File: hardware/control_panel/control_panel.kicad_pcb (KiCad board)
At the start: 2 copper layers, 13.5 x 21.5 mm, 2 parts, among them SW1 RotaryEncoder_Switch_MP

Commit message: KiCad updates and EC11 to TWT
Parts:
- removed SW1: RotaryEncoder_Switch_MP, Rotary_Encoder:RotaryEncoder_Alps_EC11E-Switch_Vertical_H20mm
- added 5VGND1: Conn_01x02_Pin, Connector_JST:JST_XH_B2B-XH-A_1x02_P2.50mm_Vertical, F.Cu at (53.3, 53.0)
- added R1: 10k, Resistor_THT:R_Axial_DIN0204_L3.6mm_D1.6mm_P5.08mm_Horizontal, F.Cu at (123.1, 36.5)
- added R2: 10k, Resistor_THT:R_Axial_DIN0204_L3.6mm_D1.6mm_P5.08mm_Horizontal, F.Cu at (123.1, 39.7)
- added R3: 10k, Resistor_THT:R_Axial_DIN0204_L3.6mm_D1.6mm_P5.08mm_Horizontal, F.Cu at (123.1, 42.9)
- added RELAY_2CH_1: Conn_01x04_Pin, Connector_PinHeader_2.54mm:PinHeader_1x04_P2.54mm_Vertical, F.Cu at (54.5, 80.9)
- added ST7789_Socket1: Conn_01x08_Socket, Connector_PinSocket_2.54mm:PinSocket_1x08_P2.54mm_Horizontal, F.Cu at (116.0, 77.4)
- added SW_Cancel_Reset1: SW_Push, Button_Switch_THT:SW_PUSH_6mm_H8.5mm, F.Cu at (100.5, 55.3)
- added SW_Start_Stop_Adjust1: RotaryEncoder_Switch_MP, Rotary_Encoder:RotaryEncoder_Alps_EC11E-Switch_Vertical_H20mm, F.Cu at (92.6, 72.4)
- moved ESPMC1 12.6 mm to (64.5, 68.5), turned to 90 degrees
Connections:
- ESPMC1 pad 1: unconnected-(ESPMC1-GP1-Pad1) -> /IN1_FAN
- ESPMC1 pad 10: unconnected-(ESPMC1-GP10-Pad10) -> /LCD_RST
- ESPMC1 pad 11: unconnected-(ESPMC1-GP11-Pad11) -> /LCD_SDA
- ESPMC1 pad 12: unconnected-(ESPMC1-GP12-Pad12) -> /LCD_SCL
- ESPMC1 pad 2: unconnected-(ESPMC1-GP2-Pad2) -> /IN2_LEDS
- ESPMC1 pad 3V3: unconnected-(ESPMC1-3V3(OUT)-Pad3V3) -> /3V3+
- ESPMC1 pad 4: unconnected-(ESPMC1-GP4-Pad4) -> Net-(ESPMC1-GP4)
- ESPMC1 pad 5: unconnected-(ESPMC1-GP5-Pad5) -> Net-(ESPMC1-GP5)
- ESPMC1 pad 5V: unconnected-(ESPMC1-Pad5V) -> Net-(5VGND1-Pin_1)
- ESPMC1 pad 6: unconnected-(ESPMC1-GP6-Pad6) -> Net-(ESPMC1-GP6)
- ESPMC1 pad 7: unconnected-(ESPMC1-GP7-Pad7) -> Net-(ESPMC1-GP7)
- ESPMC1 pad 8: unconnected-(ESPMC1-GP8-Pad8) -> /LCD_BL
- ESPMC1 pad 9: unconnected-(ESPMC1-GP9-Pad9) -> /LCD_DC
- ESPMC1 pad GND: unconnected-(ESPMC1-PadGND) -> GND
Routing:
- net /3V3+: track 0.00 -> 55.9 mm, vias 0 -> 1
- net Net-(5VGND1-Pin_1): track 0.00 -> 8.31 mm, vias 0 -> 1
- net GND: track 0.00 -> 8.29 mm, vias 0 -> 1
- net /IN2_LEDS: track 0.00 -> 4.81 mm, vias 0 -> 1
- net /IN1_FAN: track 0.00 -> 4.76 mm, vias 0 -> 1
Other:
- board size 13.5 x 21.5 mm -> 70 x 37 mm

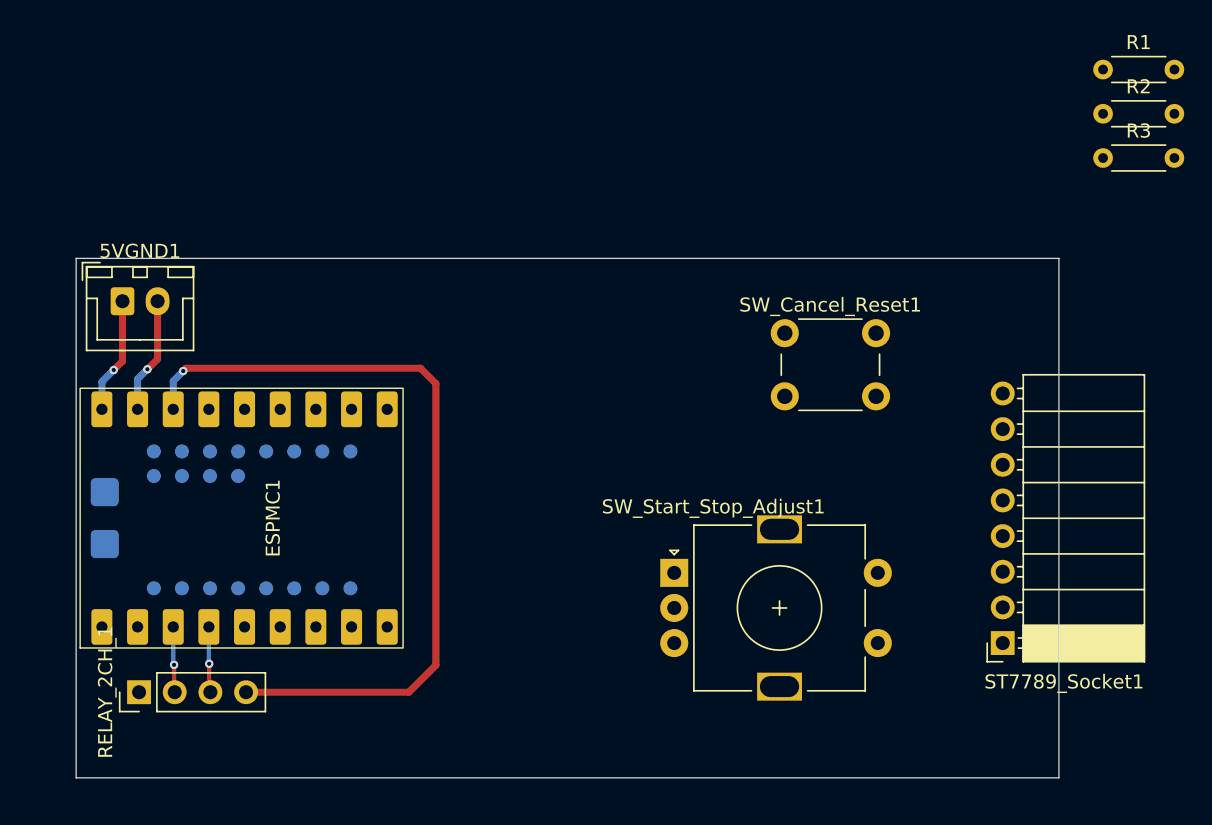
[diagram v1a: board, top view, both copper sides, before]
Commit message: KiCad and python script for stitching PCB layers into one SVG for printing
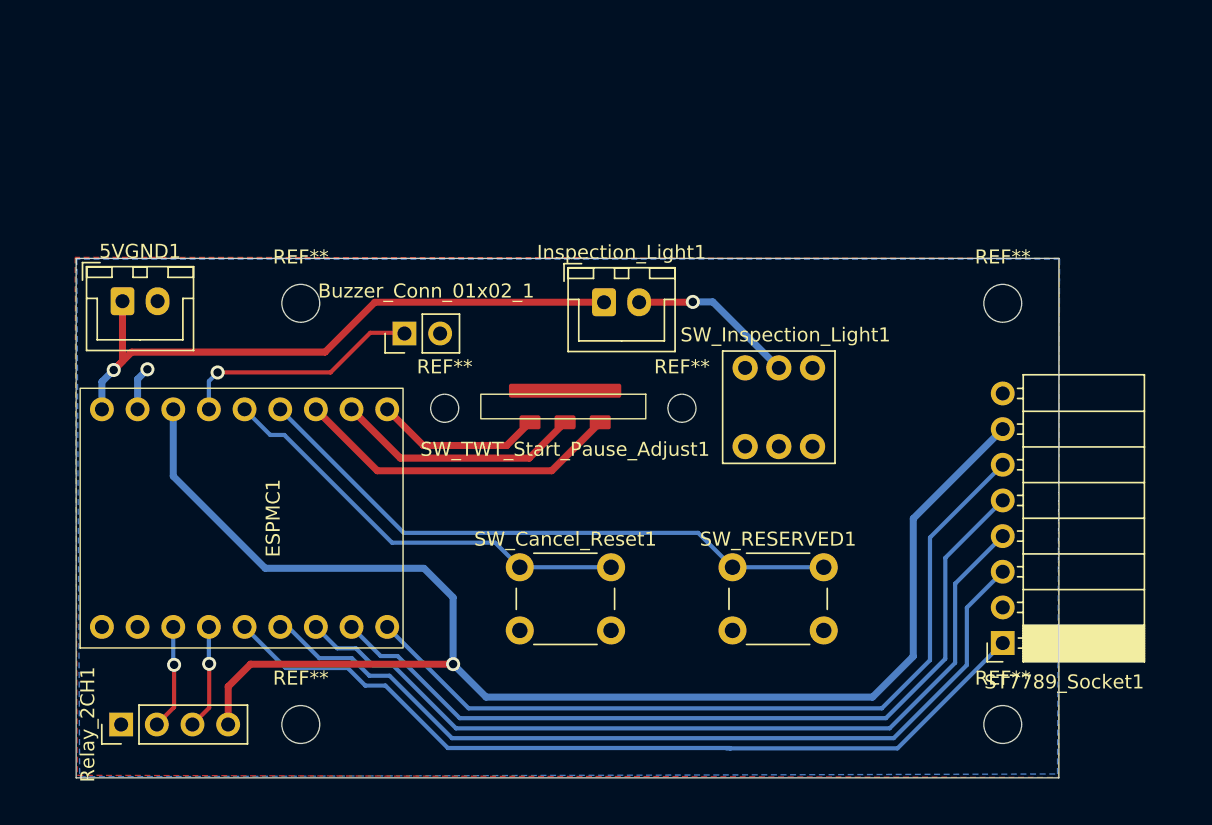
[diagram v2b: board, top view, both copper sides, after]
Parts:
- removed R1, R2, R3: 10k, Resistor_THT:R_Axial_DIN0204_L3.6mm_D1.6mm_P5.08mm_Horizontal
- removed SW_Start_Stop_Adjust1: RotaryEncoder_Switch_MP, Rotary_Encoder:RotaryEncoder_Alps_EC11E-Switch_Vertical_H20mm
- added Buzzer_Conn_01x02_1: Buzzer, Connector_PinHeader_2.54mm:PinHeader_1x02_P2.54mm_Vertical, F.Cu at (73.4, 55.4)
- added Inspection_Light1: Conn_01x02_Socket, Connector_JST:JST_XH_B2B-XH-A_1x02_P2.50mm_Vertical, F.Cu at (87.6, 53.1)
- added REF**: MountingHole_2mm, MountingHole:MountingHole_2mm, F.Cu at (76.2, 60.7)
- added REF**: MountingHole_2.7mm_M2.5_DIN965, MountingHole:MountingHole_2.7mm_M2.5_DIN965, F.Cu at (116.0, 83.2)
- added REF**: MountingHole_2.7mm_M2.5_DIN965, MountingHole:MountingHole_2.7mm_M2.5_DIN965, F.Cu at (66.0, 53.2)
- added REF**: MountingHole_2.7mm_M2.5_DIN965, MountingHole:MountingHole_2.7mm_M2.5_DIN965, F.Cu at (116.0, 53.2)
- added REF**: MountingHole_2.7mm_M2.5_DIN965, MountingHole:MountingHole_2.7mm_M2.5_DIN965, F.Cu at (66.0, 83.2)
- added REF**: MountingHole_2mm, MountingHole:MountingHole_2mm, F.Cu at (93.2, 60.7)
- added SW_Inspection_Light1: SW_Push_DPDT, TMB_Library:SW_Push_DPDT_8x8mm, F.Cu at (100.0, 60.6)
- added SW_RESERVED1: SW_Push, Button_Switch_THT:SW_PUSH_6mm_H8.5mm, F.Cu at (96.8, 72.0)
- added SW_TWT_Start_Pause_Adjust1: ~, TMB_Library:SW_ThumbWheelToggle, F.Cu at (84.8, 60.7)
- ESPMC1: footprint TMB_Library:ESP32-S3_Super_Mini -> TMB_Library:ESP32-S3_Super_Mini_THTONLY
- moved SW_Cancel_Reset1 25.2 mm to (81.6, 72.0)
- moved Relay_2CH1 2.63 mm to (53.2, 83.2)
- renumbered RELAY_2CH_1 to Relay_2CH1
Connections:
- net Net-(5VGND1-Pin_1) renamed /+5V
- ESPMC1 pad 10: /LCD_RST -> /WH_DIR2
- ESPMC1 pad 11: /LCD_SDA -> /RESERVED
- ESPMC1 pad 12: /LCD_SCL -> /CNCL_RSET
- ESPMC1 pad 13: unconnected-(ESPMC1-GP13-Pad13) -> /BUZZER
- ESPMC1 pad 3: unconnected-(ESPMC1-GP3-Pad3) -> /LCD_BL
- ESPMC1 pad 4: Net-(ESPMC1-GP4) -> /LCD_DC
- ESPMC1 pad 5: Net-(ESPMC1-GP5) -> /LCD_RST
- ESPMC1 pad 6: Net-(ESPMC1-GP6) -> /LCD_SDA
- ESPMC1 pad 7: Net-(ESPMC1-GP7) -> /LCD_SCL
- ESPMC1 pad 8: /LCD_BL -> /WH_DIR1
- ESPMC1 pad 9: /LCD_DC -> /WH_SW
- SW_Cancel_Reset1 pad 1: GND -> /CNCL_RSET
- SW_Cancel_Reset1 pad 2: Net-(ESPMC1-GP4) -> GND
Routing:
- net /LCD_DC: track 0.00 -> 62.1 mm
- net /LCD_BL: track 0.00 -> 61.0 mm
- net /LCD_RST: track 0.00 -> 60.9 mm
- net /LCD_SDA: track 0.00 -> 59.7 mm
- net /LCD_SCL: track 0.00 -> 58.5 mm
- net /3V3+: track 55.9 -> 106.2 mm
- net /RESERVED: track 0.00 -> 43.5 mm
- net /+5V: track 8.31 -> 45.2 mm
- net /CNCL_RSET: track 0.00 -> 30.8 mm
- net /WH_DIR2: track 0.00 -> 23.5 mm
- net /WH_SW: track 0.00 -> 17.7 mm
- net /BUZZER: track 0.00 -> 17.4 mm, vias 0 -> 1
- net /WH_DIR1: track 0.00 -> 11.9 mm
- net /INSP_LIGHT_GND: track 0.00 -> 11.9 mm, vias 0 -> 1
- net GND: track 8.29 -> 3.14 mm
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- added copper zone on B.Cu, net GND
- added copper zone on F.Cu, net GND

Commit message: KiCad design fixes and Kicad pcb export fixes
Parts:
- Inspection_Light1: footprint Connector_JST:JST_XH_B2B-XH-A_1x02_P2.50mm_Vertical -> Connector_PinHeader_2.54mm:PinHeader_1x02_P2.54mm_Vertical
- moved Relay_2CH1 58.4 mm to (108.6, 64.6), turned to 0 degrees
- moved Inspection_Light1 21.0 mm to (108.6, 54.2)
- moved REF** 3.00 mm to (63.0, 53.2)
- moved REF** 3.00 mm to (63.0, 83.2)
- moved SW_Cancel_Reset1 2.01 mm to (81.2, 74.0)
- moved SW_RESERVED1 2.00 mm to (96.8, 74.0)
- renumbered ESPMC1 to ESP32-S3SM1
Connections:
- ESP32-S3SM1 pad 1: /IN1_FAN -> /RESERVED
- ESP32-S3SM1 pad 10: /WH_DIR2 -> /WH_DIR1
- ESP32-S3SM1 pad 11: /RESERVED -> /IN1_FAN
- ESP32-S3SM1 pad 12: /CNCL_RSET -> /IN2_LEDS
- ESP32-S3SM1 pad 2: /IN2_LEDS -> /CNCL_RSET
- ESP32-S3SM1 pad 3: /LCD_BL -> /LCD_SCL
- ESP32-S3SM1 pad 4: /LCD_DC -> /LCD_SDA
- ESP32-S3SM1 pad 6: /LCD_SDA -> /LCD_DC
- ESP32-S3SM1 pad 7: /LCD_SCL -> /LCD_BL
- ESP32-S3SM1 pad 8: /WH_DIR1 -> /WH_DIR2
- Inspection_Light1 pad 1: /+5V -> /INSP_LITE_5+
- Inspection_Light1 pad 2: /INSP_LIGHT_GND -> GND
- ST7789_Socket1 pad 1: /LCD_BL -> GND
- ST7789_Socket1 pad 2: GND -> /3V3+
- ST7789_Socket1 pad 3: /LCD_DC -> /LCD_SCL
- ST7789_Socket1 pad 4: /LCD_RST -> /LCD_SDA
- ST7789_Socket1 pad 5: /LCD_SDA -> /LCD_RST
- ST7789_Socket1 pad 6: /LCD_SCL -> /LCD_DC
- ST7789_Socket1 pad 7: /3V3+ -> GND
- ST7789_Socket1 pad 8: GND -> /LCD_BL
- SW_Cancel_Reset1 pad 1: /CNCL_RSET -> GND
- SW_Cancel_Reset1 pad 2: GND -> /CNCL_RSET
- SW_Inspection_Light1 pad 4: GND -> /INSP_LITE_5+
- SW_Inspection_Light1 pad 5: /INSP_LIGHT_GND -> /+5V
- SW_RESERVED1 pad 1: /RESERVED -> GND
- SW_RESERVED1 pad 2: GND -> /RESERVED
- SW_TWT_Start_Pause_Adjust1 pad 1: /WH_DIR2 -> /WH_DIR1
- SW_TWT_Start_Pause_Adjust1 pad 3: /WH_DIR1 -> /WH_DIR2
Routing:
- net /IN2_LEDS: track 7.57 -> 50.3 mm, vias 1 -> 0
- net /3V3+: track 106.2 -> 66.3 mm
- net /IN1_FAN: track 7.55 -> 46.8 mm, vias 1 -> 0
- net /+5V: track 45.2 -> 59.6 mm
- net /INSP_LIGHT_GND: track 11.9 -> 0.00 mm, vias 1 -> 0
- net /WH_DIR2: track 23.5 -> 11.9 mm
- net /WH_DIR1: track 11.9 -> 23.5 mm
- net /INSP_LITE_5+: track 0.00 -> 8.66 mm, vias 0 -> 1
- net /LCD_SCL: track 58.5 -> 65.8 mm, vias 0 -> 1
- net /RESERVED: track 43.5 -> 49.0 mm, vias 0 -> 1
- net /LCD_SDA: track 59.7 -> 65.2 mm, vias 0 -> 1
- net GND: track 3.14 -> 8.29 mm
- net /LCD_BL: track 61.0 -> 63.6 mm, vias 0 -> 1
- net /LCD_RST: track 60.9 -> 63.4 mm, vias 0 -> 1
- net /BUZZER: track 17.4 -> 16.2 mm, vias 1 -> 0
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
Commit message: Minimum vias - 0.3mm tracks
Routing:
- net /RESERVED: track 49.0 -> 50.1 mm, vias 1 -> 0
- net /CNCL_RSET: track 30.4 -> 31.2 mm, vias 1 -> 0
- net /+5V: track 59.6 -> 60.4 mm, vias 1 -> 0
- net /3V3+: track 66.3 -> 65.6 mm, vias 1 -> 0
- net /INSP_LITE_5+: track 8.66 -> 8.94 mm, vias 1 -> 0
- net /LCD_SDA: vias 1 -> 0
- net /LCD_SCL: vias 1 -> 0
- net GND: vias 1 -> 0
- net /LCD_RST: vias 1 -> 0
- net /LCD_DC: vias 1 -> 0
- net /LCD_BL: vias 1 -> 0

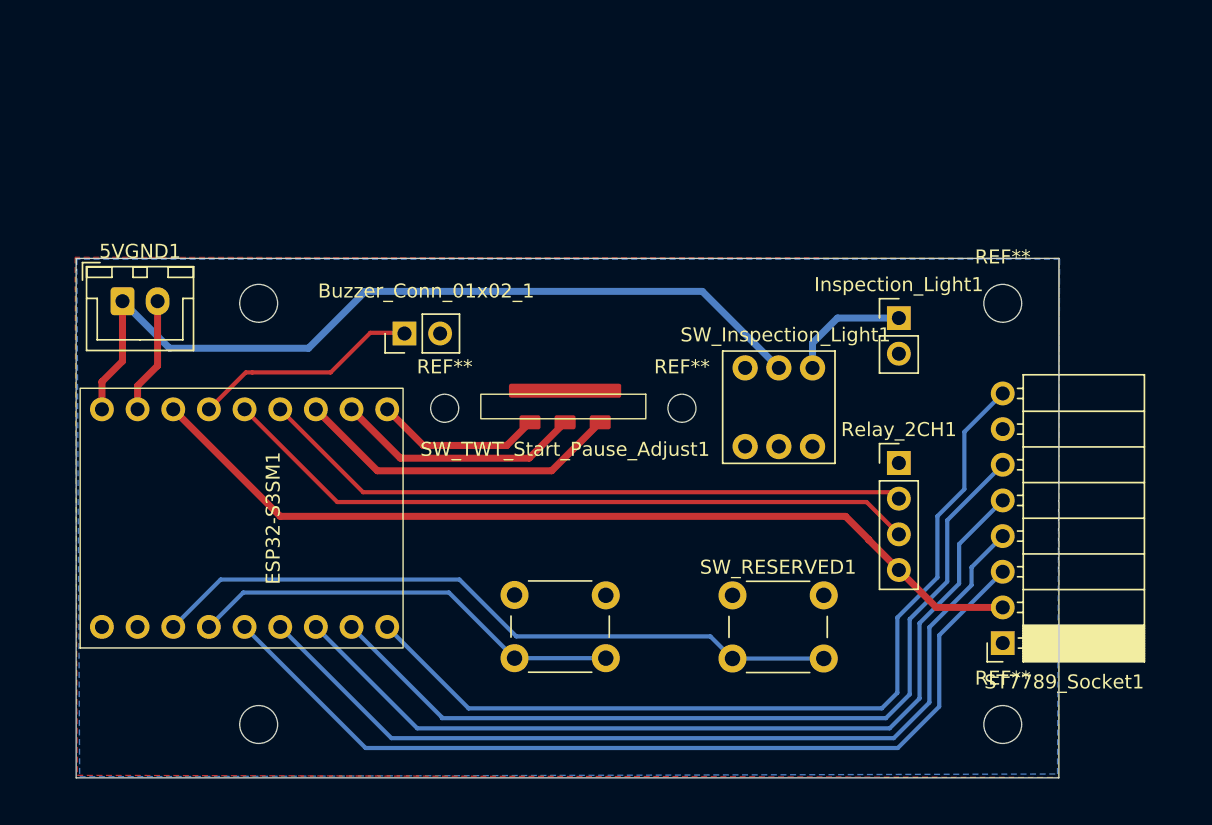
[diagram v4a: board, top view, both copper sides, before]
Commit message: Kicad - Mimimum Vias + 0.5mm min track width + script changes
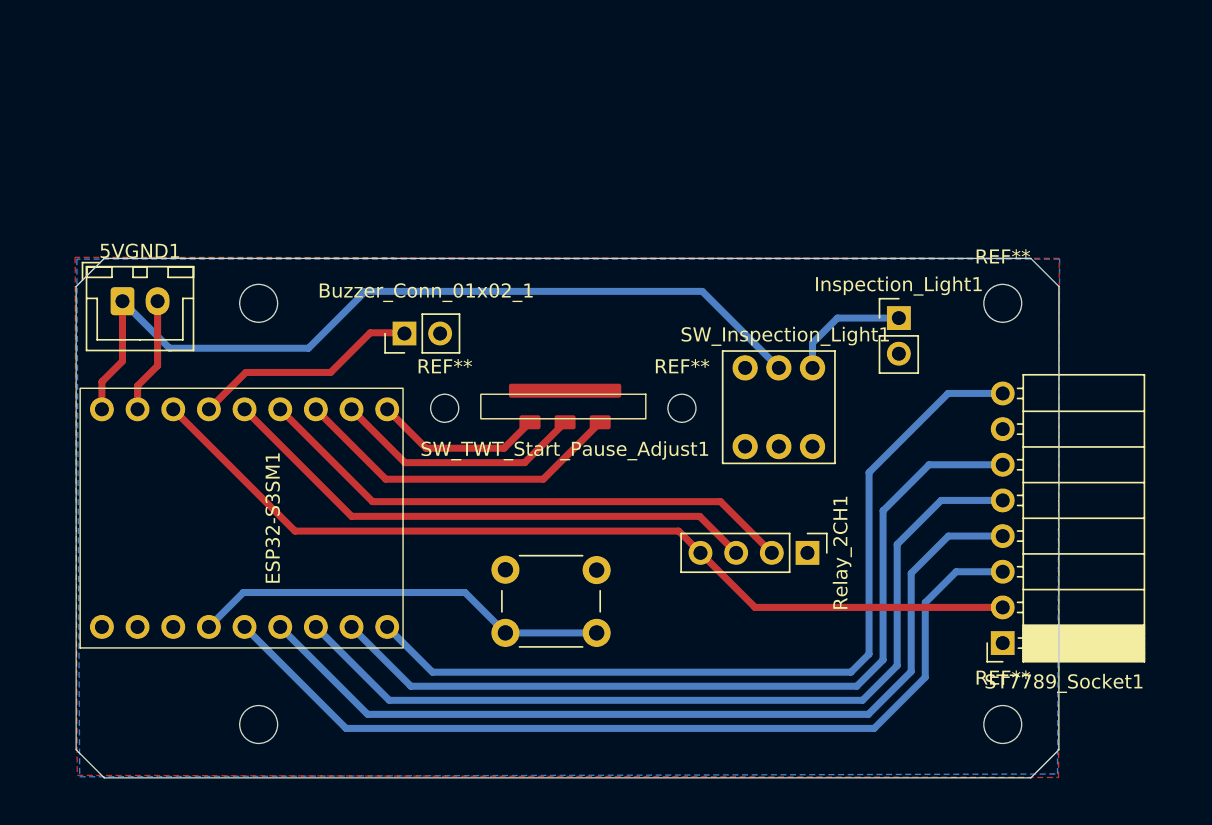
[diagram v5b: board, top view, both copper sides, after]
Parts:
- removed SW_RESERVED1: SW_Push, Button_Switch_THT:SW_PUSH_6mm_H8.5mm
- moved Relay_2CH1 9.13 mm to (102.1, 71.0), turned to -90 degrees
- moved SW_Cancel_Reset1 1.91 mm to (80.6, 72.2)
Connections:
- ESP32-S3SM1 pad 1: /RESERVED -> unconnected-(ESP32-S3SM1-GP1-Pad1)
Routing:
- net /RESERVED: track 50.1 -> 0.00 mm
- net /IN2_LEDS: track 50.3 -> 39.3 mm
- net /IN1_FAN: track 46.8 -> 39.3 mm
- net /LCD_BL: track 63.6 -> 61.0 mm
- net /LCD_SDA: track 65.2 -> 63.4 mm
- net /CNCL_RSET: track 31.2 -> 29.8 mm
- net /LCD_DC: track 62.3 -> 60.9 mm
- net /LCD_RST: track 63.4 -> 62.0 mm
- net /LCD_SCL: track 65.8 -> 64.7 mm
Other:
- outline, holes or cut-outs redrawn

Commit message: KiCad changes
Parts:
- removed the REF** at (76.2, 60.7)
- removed the REF** at (93.2, 60.7)
- moved Buzzer_Conn_01x02_1 33.5 mm to (54.4, 83.0)
- moved Relay_2CH1 29.0 mm to (78.4, 54.1)
- moved Inspection_Light1 24.0 mm to (94.2, 73.4)
- moved SW_Inspection_Light1 13.5 mm to (101.2, 74.1)
- moved SW_TWT_Start_Pause_Adjust1 0.83 mm to (85.7, 60.6)
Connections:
- net /INSP_LITE_5+ renamed /INSP_LITE_3.3V+
- ESP32-S3SM1 pad 1: unconnected-(ESP32-S3SM1-GP1-Pad1) -> /BUZZER
- ESP32-S3SM1 pad 11: /IN1_FAN -> unconnected-(ESP32-S3SM1-GP11-Pad11)
- ESP32-S3SM1 pad 12: /IN2_LEDS -> /IN1_FAN
- ESP32-S3SM1 pad 13: /BUZZER -> /IN2_LEDS
- SW_Inspection_Light1 pad 5: /+5V -> /3V3+
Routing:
- net /+5V: track 60.4 -> 8.31 mm
- net /IN1_FAN: track 39.3 -> 16.6 mm
- net /IN2_LEDS: track 39.3 -> 16.7 mm
- net /3V3+: track 65.6 -> 85.2 mm
- net /BUZZER: track 16.2 -> 7.78 mm
- net /WH_DIR2: track 12.1 -> 14.4 mm
- net /INSP_LITE_3.3V+: track 8.94 -> 10.3 mm
- net /WH_DIR1: track 24.0 -> 24.8 mm
- net /WH_SW: track 18.0 -> 18.8 mm
